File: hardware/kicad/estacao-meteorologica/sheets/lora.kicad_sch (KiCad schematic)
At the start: 8 parts, among them J70 U.FL / 50 ohm, U12 LORA1276-C1-915MHZ

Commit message: Padronizacao de nomes e numero de componentes
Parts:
- C701: renamed from C11; value 100n -> 100 nF; Assembly (none) -> SMT; Function (none) -> Capacitor de desacoplamento ou filtro local.; LCSC Part C14663 -> (none); Modelo 3D ${KICAD9_3DMODEL_DIR}/Capacitor_SMD.3dshapes/C_0603_1608Met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 -> (none); Specification (none) -> 100 nF; Status_Ficha Conferido no catalogo em 2026-09-24; verificar estoque ao c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 -> (none); Verification (none) -> Conferido no catalogo em 2026-09-24; verificar estoque ao c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
- C702: renamed from C12; value 10u -> 10 µF; Assembly (none) -> SMT; Function (none) -> Capacitor de desacoplamento ou filtro local.; LCSC Part C13585 -> (none); Modelo 3D ${KICAD9_3DMODEL_DIR}/Capacitor_SMD.3dshapes/C_1206_3216Met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 -> (none); Specification (none) -> 10 µF; Status_Ficha Conferido no catalogo em 2026-09-24; verificar estoque ao c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 -> (none); Verification (none) -> Conferido no catalogo em 2026-09-24; verificar estoque ao c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
- D701: renamed from D70; Assembly (none) -> SMT; Function (none) -> Diodo de proteção ou clamp.; LCSC Part C461221 -> (none); Modelo 3D ${KIPRJMOD}/../../libraries/Hardware_LoRa/Hardware_LoRa.3ds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 -> (none); Specification (none) -> PESD5V0R1BSFYL; Status_Ficha Conferido no catalogo em 2026-09-24; verificar estoque ao c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 -> (none); Verification (none) -> Conferido no catalogo em 2026-09-24; verificar estoque ao c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
- FB701: renamed from FB70; value 120R @100MHz / 2A -> 120 Ω @ 100 MHz, 2 A; Assembly (none) -> SMT; Function (none) -> Filtro de ferrite na alimentação.; LCSC Part C14709 -> (none); Modelo 3D ${KICAD9_3DMODEL_DIR}/Inductor_SMD.3dshapes/L_0603_1608Metr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 -> (none); Specification (none) -> 120 Ω @ 100 MHz, 2 A; Status_Ficha Conferido no catalogo em 2026-09-24; verificar estoque ao c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 -> (none); Verification (none) -> Conferido no catalogo em 2026-09-24; verificar estoque ao c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
- J701: renamed from J70; value U.FL / 50 ohm -> U.FL, 50 Ω; Assembly (none) -> SMT; Function (none) -> Conector de interface.; LCSC Part C88373 -> (none); Modelo 3D ${KIPRJMOD}/../../libraries/Hardware_LoRa/Hardware_LoRa.3ds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 -> (none); Specification (none) -> U.FL, 50 Ω; Status_Ficha Conferido no catalogo em 2026-09-24; verificar estoque ao c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 -> (none); Verification (none) -> Conferido no catalogo em 2026-09-24; verificar estoque ao c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
- R701: renamed from R14; value 10k -> 10 kΩ; Assembly (none) -> SMT; Function (none) -> Resistor de polarização, filtro ou configuração.; LCSC Part C25804 -> (none); Modelo 3D ${KICAD9_3DMODEL_DIR}/Resistor_SMD.3dshapes/R_0603_1608Metr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 -> (none); Specification (none) -> 10 kΩ; Status_Ficha Conferido no catalogo em 2026-09-24; verificar estoque ao c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 -> (none); Verification (none) -> Conferido no catalogo em 2026-09-24; verificar estoque ao c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
- R702: renamed from R15; value 10k -> 10 kΩ; Assembly (none) -> SMT; Function (none) -> Resistor de polarização, filtro ou configuração.; LCSC Part C25804 -> (none); Modelo 3D ${KICAD9_3DMODEL_DIR}/Resistor_SMD.3dshapes/R_0603_1608Metr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 -> (none); Specification (none) -> 10 kΩ; Status_Ficha Conferido no catalogo em 2026-09-24; verificar estoque ao c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 -> (none); Verification (none) -> Conferido no catalogo em 2026-09-24; verificar estoque ao c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
- U701: renamed from U12; Assembly (none) -> SMT; Function (none) -> Circuito integrado ou módulo funcional.; LCSC Part C3001531 -> (none); Modelo 3D ${KIPRJMOD}/../../libraries/Hardware_LoRa/Hardware_LoRa.3ds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 -> (none); Specification (none) -> LORA1276-C1-915MHZ; Status_Ficha Conferido no catalogo em 2026-09-24; verificar estoque ao c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 -> (none); Verification (none) -> Conferido no catalogo em 2026-09-24; verificar estoque ao c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
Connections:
- net Lora_DIO0 renamed LORA_DIO0
- net Lora_DIO1 renamed LORA_DIO1
- net Lora_DIO2 renamed LORA_DIO2
- net Lora_MISO renamed LORA_SPI_MISO
- net Lora_MOSI renamed LORA_SPI_MOSI
- net Lora_NSS renamed LORA_NSS
- net Lora_RST renamed LORA_RST
- net Lora_SCK renamed LORA_SPI_SCK
- net VCC_LORA renamed +3V3_LORA

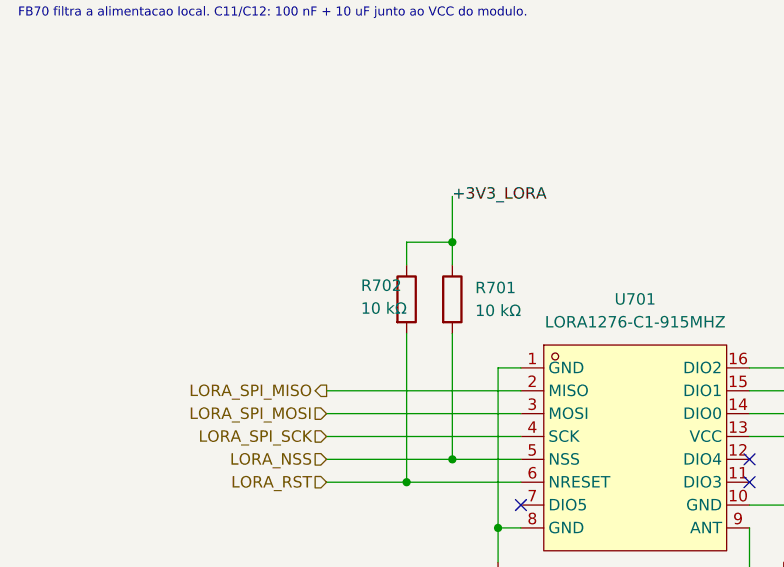
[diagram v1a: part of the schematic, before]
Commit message: Ajuste de componentes por folha
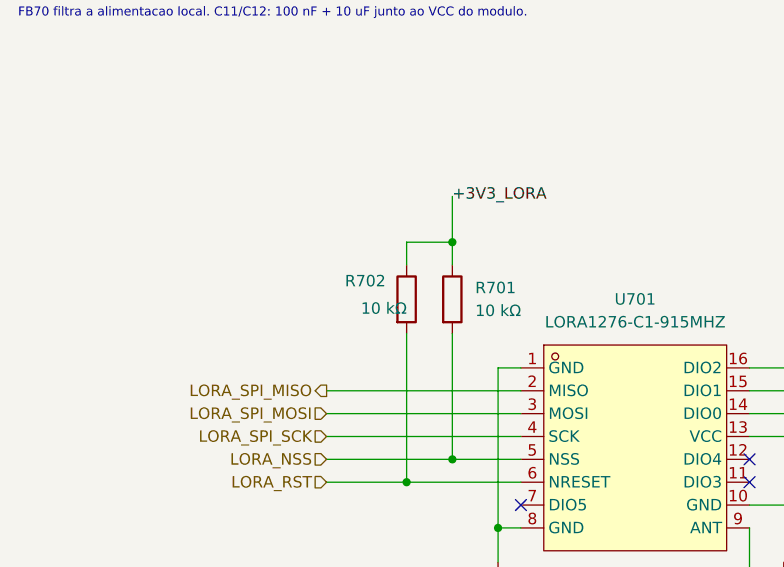
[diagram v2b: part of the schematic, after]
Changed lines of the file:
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@@
+			)
+		)
+		(property "Function" "Circuito integrado ou módulo funcional."
+			(at 0 0 0)
+			(effects
+				(font
+					(size 1.27 1.27)
+				)
+				(hide yes)
+			)
+		)
+		(property "Specification" "LORA1276-C1-915MHZ"
+			(at 0 0 0)
+			(effects
+				(font
+					(size 1.27 1.27)
+				)
+				(hide yes)
+			)
+		)
+		(property "Assembly" "SMT"
+			(at 0 0 0)
+			(effects
+				(font
+					(size 1.27 1.27)
+				)
+				(hide yes)
 			)
 		)
@@
 					(unit 1)
 				)
-			)
-		)
-		(property "Function" "Circuito integrado ou módulo funcional."
-			(at 0 0 0)
-			(effects
-				(font (size 1.27 1.27))
-				(hide yes)
-			)
-		)
-		(property "Specification" "LORA1276-C1-915MHZ"
-			(at 0 0 0)
-			(effects
-				(font (size 1.27 1.27))
-				(hide yes)
-			)
-		)
-		(property "Assembly" "SMT"
-			(at 0 0 0)
-			(effects
-				(font (size 1.27 1.27))
-				(hide yes)
 			)
 		)
@@
 			)
 		)
+		(property "Function" "Capacitor de desacoplamento ou filtro local."
+			(at 0 0 0)
+			(effects
+				(font
+					(size 1.27 1.27)
+				)
+				(hide yes)
+			)
+		)
+		(property "Specification" "100 nF"
+			(at 0 0 0)
+			(effects
+				(font
+					(size 1.27 1.27)
+				)
+				(hide yes)
+			)
+		)
+		(property "Assembly" "SMT"
+			(at 0 0 0)
+			(effects
+				(font
+					(size 1.27 1.27)
+				)
+				(hide yes)
+			)
+		)
 		(pin "1"
 		)
@@
 					(unit 1)
 				)
-			)
-		)
-		(property "Function" "Capacitor de desacoplamento ou filtro local."
-			(at 0 0 0)
-			(effects
-				(font (size 1.27 1.27))
-				(hide yes)
-			)
-		)
-		(property "Specification" "100 nF"
-			(at 0 0 0)
-			(effects
-				(font (size 1.27 1.27))
-				(hide yes)
-			)
-		)
-		(property "Assembly" "SMT"
-			(at 0 0 0)
-			(effects
-				(font (size 1.27 1.27))
-				(hide yes)
 			)
 		)
@@
 		(dnp no)
 		(property "Reference" "R702"
-			(at 114.3 73.406 0)
+			(at 112.522 72.898 0)
 			(effects
 				(font
@@
 		(property "Verification" "Conferido no catalogo em 2026-09-24; verificar estoque ao comprar"
 			(at 119.38 74.93 0)
+			(effects
+				(font
+					(size 1.27 1.27)
+				)
+				(hide yes)
+			)
+		)
+		(property "Function" "Resistor de polarização, filtro ou configuração."
+			(at 0 0 0)
+			(effects
+				(font
+					(size 1.27 1.27)
+				)
+				(hide yes)
+			)
+		)
+		(property "Specification" "10 kΩ"
+			(at 0 0 0)
+			(effects
+				(font
+					(size 1.27 1.27)
+				)
+				(hide yes)
+			)
+		)
+		(property "Assembly" "SMT"
+			(at 0 0 0)
 			(effects
 				(font
@@
 					(unit 1)
 				)
-			)
-		)
-		(property "Function" "Resistor de polarização, filtro ou configuração."
-			(at 0 0 0)
-			(effects
-				(font (size 1.27 1.27))
-				(hide yes)
-			)
-		)
-		(property "Specification" "10 kΩ"
-			(at 0 0 0)
-			(effects
-				(font (size 1.27 1.27))
-				(hide yes)
-			)
-		)
-		(property "Assembly" "SMT"
-			(at 0 0 0)
-			(effects
-				(font (size 1.27 1.27))
-				(hide yes)
 			)
 		)
@@
 			)
 		)
+		(property "Function" "Diodo de proteção ou clamp."
+			(at 0 0 0)
+			(effects
+				(font
+					(size 1.27 1.27)
+				)
+				(hide yes)
+			)
+		)
+		(property "Specification" "PESD5V0R1BSFYL"
+			(at 0 0 0)
+			(effects
+				(font
+					(size 1.27 1.27)
+				)
+				(hide yes)
+			)
+		)
+		(property "Assembly" "SMT"
+			(at 0 0 0)
+			(effects
+				(font
+					(size 1.27 1.27)
+				)
+				(hide yes)
+			)
+		)
 		(pin "2"
 		)
@@
 					(unit 1)
 				)
-			)
-		)
-		(property "Function" "Diodo de proteção ou clamp."
-			(at 0 0 0)
-			(effects
-				(font (size 1.27 1.27))
-				(hide yes)
-			)
-		)
-		(property "Specification" "PESD5V0R1BSFYL"
-			(at 0 0 0)
-			(effects
-				(font (size 1.27 1.27))
-				(hide yes)
-			)
-		)
-		(property "Assembly" "SMT"
-			(at 0 0 0)
-			(effects
-				(font (size 1.27 1.27))
-				(hide yes)
 			)
 		)
@@
 			)
 		)
+		(property "Function" "Capacitor de desacoplamento ou filtro local."
+			(at 0 0 0)
+			(effects
+				(font
+					(size 1.27 1.27)
+				)
+				(hide yes)
+			)
+		)
+		(property "Specification" "10 µF"
+			(at 0 0 0)
+			(effects
+				(font
+					(size 1.27 1.27)
+				)
+				(hide yes)
+			)
+		)
+		(property "Assembly" "SMT"
+			(at 0 0 0)
+			(effects
+				(font
+					(size 1.27 1.27)
+				)
+				(hide yes)
+			)
+		)
 		(pin "1"
 		)
@@
 					(unit 1)
 				)
-			)
-		)
-		(property "Function" "Capacitor de desacoplamento ou filtro local."
-			(at 0 0 0)
-			(effects
-				(font (size 1.27 1.27))
-				(hide yes)
-			)
-		)
-		(property "Specification" "10 µF"
-			(at 0 0 0)
-			(effects
-				(font (size 1.27 1.27))
-				(hide yes)
-			)
-		)
-		(property "Assembly" "SMT"
-			(at 0 0 0)
-			(effects
-				(font (size 1.27 1.27))
-				(hide yes)
 			)
 		)
@@
 			)
 		)
+		(property "Function" "Resistor de polarização, filtro ou configuração."
+			(at 0 0 0)
+			(effects
+				(font
+					(size 1.27 1.27)
+				)
+				(hide yes)
+			)
+		)
+		(property "Specification" "10 kΩ"
+			(at 0 0 0)
+			(effects
+				(font
+					(size 1.27 1.27)
+				)
+				(hide yes)
+			)
+		)
+		(property "Assembly" "SMT"
+			(at 0 0 0)
+			(effects
+				(font
+					(size 1.27 1.27)
+				)
+				(hide yes)
+			)
+		)
 		(pin "2"
 		)
@@
 					(unit 1)
 				)
-			)
-		)
-		(property "Function" "Resistor de polarização, filtro ou configuração."
-			(at 0 0 0)
-			(effects
-				(font (size 1.27 1.27))
-				(hide yes)
-			)
-		)
-		(property "Specification" "10 kΩ"
-			(at 0 0 0)
-			(effects
-				(font (size 1.27 1.27))
-				(hide yes)
-			)
-		)
-		(property "Assembly" "SMT"
-			(at 0 0 0)
-			(effects
-				(font (size 1.27 1.27))
-				(hide yes)
 			)
 		)
@@
 			)
 		)
+		(property "Function" "Conector de interface."
+			(at 0 0 0)
+			(effects
+				(font
+					(size 1.27 1.27)
+				)
+				(hide yes)
+			)
+		)
+		(property "Specification" "U.FL, 50 Ω"
+			(at 0 0 0)
+			(effects
+				(font
+					(size 1.27 1.27)
+				)
+				(hide yes)
+			)
+		)
+		(property "Assembly" "SMT"
+			(at 0 0 0)
+			(effects
+				(font
+					(size 1.27 1.27)
+				)
+				(hide yes)
+			)
+		)
 		(pin "2"
 		)
@@
 					(unit 1)
 				)
-			)
-		)
-		(property "Function" "Conector de interface."
-			(at 0 0 0)
-			(effects
-				(font (size 1.27 1.27))
-				(hide yes)
-			)
-		)
-		(property "Specification" "U.FL, 50 Ω"
-			(at 0 0 0)
-			(effects
-				(font (size 1.27 1.27))
-				(hide yes)
-			)
-		)
-		(property "Assembly" "SMT"
-			(at 0 0 0)
-			(effects
-				(font (size 1.27 1.27))
-				(hide yes)
 			)
 		)
@@
 			)
 		)
+		(property "Function" "Filtro de ferrite na alimentação."
+			(at 0 0 0)
+			(effects
+				(font
+					(size 1.27 1.27)
+				)
+				(hide yes)
+			)
+		)
+		(property "Specification" "120 Ω @ 100 MHz, 2 A"
+			(at 0 0 0)
+			(effects
+				(font
+					(size 1.27 1.27)
+				)
+				(hide yes)
+			)
+		)
+		(property "Assembly" "SMT"
+			(at 0 0 0)
+			(effects
+				(font
+					(size 1.27 1.27)
+				)
+				(hide yes)
+			)
+		)
 		(pin "1"
 		)
@@
 			)
 		)
-		(property "Function" "Filtro de ferrite na alimentação."
-			(at 0 0 0)
-			(effects
-				(font (size 1.27 1.27))
-				(hide yes)
-			)
-		)
-		(property "Specification" "120 Ω @ 100 MHz, 2 A"
-			(at 0 0 0)
-			(effects
-				(font (size 1.27 1.27))
-				(hide yes)
-			)
-		)
-		(property "Assembly" "SMT"
-			(at 0 0 0)
-			(effects
-				(font (size 1.27 1.27))
-				(hide yes)
-			)
-		)
